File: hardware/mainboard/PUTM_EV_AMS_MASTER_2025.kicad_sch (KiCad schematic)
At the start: 41 parts, among them IC11 ISO6760, IC7 ISO6760, IC8 3.3V/0.5A, J1 M80-5100642, J10 M300-MV10345M1, J12 M80-51034XX, J2 USB_C_Receptacle_USB2.0_14P, J3 M80-51014XX, J4 FTSH-107-01-L-D-K, J5 M80-51004XX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

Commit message: sync
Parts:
- removed J2: USB_C_Receptacle_USB2.0_14P, Connector_USB:USB_C_Receptacle_JAE_DX07S024WJ3R400, symbol Connector:USB_C_Receptacle_USB2.0_14P
- removed J3: M80-51014XX, Samacsys:M80-51014YY, symbol Samacsys_kicad_sym:M80-51014XX
- removed R91, R92: 5.1k, Resistor_SMD:R_0603_1608Metric, symbol Device:R_Small
- removed T1: >100kHz, Samacsys:SOP254P914X350-4N, symbol Samacsys_kicad_sym:ESMIT-4180_C
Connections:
- net TSMS: now also J12.15 (Pin_15); no longer J12.1 (Pin_1)
- net ISO_COM_MOSI: no longer names the net of IC7.12 (OUTD)
- net ISO_COM_SCK: no longer names the net of IC7.11 (OUTE)
- net MCU/COM_MOSI: no longer names the net of IC7.5 (IND)
- net MCU/COM_SCK: no longer names the net of IC7.6 (INE)
- net MCU/~{COM_CS}: no longer names the net of IC7.7 (INF)
- net ~{ISO_COM_CS}: no longer names the net of IC7.10 (OUTF)
- no-connect marks 27 -> 26
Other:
- sheet Connectivity ports: added none; removed EX_D+, EX_D-
- sheet Fan Control ports: added none; removed FAN5_CTRL, FAN5_DRAIN, FAN6_CTRL, FAN6_DRAIN, FAN7_CTRL, FAN7_DRAIN
- sheet MCU ports: added none; removed COM_MOSI, COM_SCK, EN_12V, FAN5_CTRL, FAN6_CTRL, FAN7_CTRL, PG_12V, ~{COM_CS}
- sheet Power ports: added none; removed EN_12V, PG_12V
- note removed: "USB CONNECTOR"

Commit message: schematic?
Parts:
- removed C39, C44, C45, C46, C47, C48: 100nF, Capacitor_SMD:C_0603_1608Metric, symbol Device:C_Small
- removed C40, C59, C77: 22uF, Capacitor_SMD:C_0805_2012Metric, symbol Device:C_Small
- removed F6, F7: 5V/0.5A, Fuse:Fuse_0805_2012Metric, symbol Device:Polyfuse_Small
- removed IC11, IC7: ISO6760, Package_SO:SOIC-16W_7.5x10.3mm_P1.27mm, symbol Samacsys_kicad_sym:ISO6760
- removed IC8: 3.3V/0.5A, Package_TO_SOT_SMD:SOT-23-5, symbol AP7365-33YRG-13:AP7365-33YRG-13
- removed J12: M80-51034XX, Samacsys:M80-51034YY, symbol Samacsys_kicad_sym:M80-51034XX
- removed R22: 200, Resistor_SMD:R_0603_1608Metric, symbol Device:R_Small
- removed TP4, TP5, TP6, TP7, TP8: TestPoint_Small, TestPoint:TestPoint_THTPad_D1.0mm_Drill0.5mm, symbol Connector:TestPoint_Small
- removed U4: UCC12040DVE, Package_SO:SOIC-16W_7.5x10.3mm_P1.27mm, symbol Samacsys_kicad_sym:UCC12040DVE
- added C81: 100pF, Capacitor_SMD:C_0603_1608Metric, symbol Device:C_Small
- added D21, D22: 3.6V/400W, Package_TO_SOT_SMD:SOT-23-6, symbol Power_Protection:ESDA5V3SC5
- added D23: 5.3V/400W, Package_TO_SOT_SMD:SOT-23-3, symbol Power_Protection:ESDA5V3L
- added J2: M80-5102042, Samacsys:M80-51020YY, symbol Samacsys_kicad_sym:M80-5102042
- added J3: M80-5100842, Samacsys:M80-51008YY, symbol Samacsys_kicad_sym:M80-5100842
- added T1: SM91502ALE, Samacsys:SOP254P927X572-6N, symbol Samacsys_kicad_sym:SM91502ALE
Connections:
- net GNDISO is gone; now on net GND: J8.4 (Pin_4)
- net AIR_M_DETECTION: now also J2.15
- net AIR_PRE_DETECTION: now also J2.14
- net AIR_P_DETECTION: now also J2.13
- net CANFD1+: now also J2.3
- net CANFD1-: now also J2.4
- net CANFD2+: now also J2.5
- net CANFD2-: now also J2.6
- net CAR_I: now also D23.1 (K)
- net CCO+: now also T1.3 (PRI_3)
- net CCO-: now also T1.1 (PRI_1)
- net CHARGER_DETECTION: now also J2.12
- net FAN1-: now also J3.1
- net FAN2-: now also J3.2
- net FAN3-: now also J3.3
- net FAN4-: now also J3.4
- net GND: now also C81.2, D21.2 (K), D21.5 (NC), D22.2 (K), D22.5 (NC), D23.3 (A), J2.11, J2.19, J2.20
- net NRST: now also D21.4 (A)
- net SAFETY_IN: now also J2.8
- net SAFETY_OUT: now also J2.7
- net SWCLK: now also D21.3 (A)
- net SWDIO: now also D21.1 (A)
- net TSMS: now also J2.18
- net UART_RX: now also D22.1 (A)
- net UART_TX: now also D21.6 (A)
- net VDD: now also J2.10
- net +3.3V renamed +3.3VIO
- net +3.3VIO: now also D22.3 (A)
- net +5VISO: no longer names the net of J8.3 (Pin_3)
- net ACU+ renamed IsolationBarrier/ACU_IN+
- net ACU- renamed IsolationBarrier/ACU_IN-
- net CAR+ renamed IsolationBarrier/CAR_IN+
- net CAR- renamed IsolationBarrier/CAR_IN-
- net CAR_I_REF renamed +5VA
- net +5VA: now also D23.2 (K)
- new net: C81.1, T1.5 (SEC_2)
- new net +24V: J3.5, J3.6, J3.7, J3.8
- new net +8V: J2.9
- new net D+: J2.2
- new net D-: J2.1
- new net Isolated SPI/OUT+: T1.4 (SEC_1)
- new net Isolated SPI/OUT-: T1.6 (SEC_3)
- new net VBUS+: J2.17
- no-connect marks 26 -> 12
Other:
- sheet Isolated ADC renamed ADC
- added sheet IsolationBarrier (IsolationBarrier.kicad_sch)
- sheet ADC: file IsolatedADC.kicad_sch -> ADC.kicad_sch
- sheet ADC ports: added none; removed CAR_I_REF
- sheet Connectivity ports: added EX_D+, EX_D-, FTDI_RX, FTDI_TX; removed EX_USB_D+, EX_USB_D-, UC_D+, UC_D-
- sheet Isolated SPI ports: added RX, TX; removed MISO, MOSI, SCK, SPI_RDY, ~{CS}
- sheet MCU ports: added DETECT_USB, SIGNAL_LED_ERR, SIGNAL_LED_OK, SIGNAL_LED_WRN, UART_COM_RX, UART_COM_TX, UART_DEBUG_RX, UART_DEBUG_TX, UART_USB_RX, UART_USB_TX; removed COM_MISO, D+, D-, SIGNAL_LED_1, SIGNAL_LED_2, SIGNAL_LED_3, SPI_RDY, UART_RX, UART_TX
- sheet Power ports: added VBUS_SENSE; removed none
- sheet Safety ports: added none; removed DASH_LED_ERROR
- note added: "ADC"
- note added: "AIR"
- note added: "COM"
- note added: "CURRENT"
- note added: "FAN"
- note added: "USBGND"
- note removed: "ADC AND SPI"
- note removed: "AIR CONNECTORS"
- note removed: "AIR CONTROL"
- note removed: "CONNECTORS"
- note removed: "FAN CONNECTORS"
- note removed: "FAN CONTROL"
- note removed: "GALVANIC ISOLATION"
- note removed: "ISO POWER"
- note removed: "SHARED"
- note removed: "TI_IC ONLY"
- moved on the sheet: D1, D2, D3, D6, J1, J10, J4, J5, J7, J8, R27, R31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

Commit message: sync
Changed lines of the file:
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@@
+		)
+	)
+	(label "ADC_MOSI"
+		(at 182.88 81.28 180)
+		(effects
+			(font
+				(size 0.508 0.508)
+			)
+			(justify right bottom)
 		)
 	)
@@
 	)
 	(label "ADC_MISO"
-		(at 182.88 81.28 180)
+		(at 182.88 78.74 180)
 		(effects
 			(font
@@
 		)
 	)
+	(label "ADC_SCK"
+		(at 182.88 83.82 180)
+		(effects
+			(font
+				(size 0.508 0.508)
+			)
+			(justify right bottom)
+		)
+	)
 	(label "FC1"
 		(at 182.88 259.08 180)
@@
 		)
 	)
-	(label "ADC_MISO"
-		(at 182.88 78.74 180)
-		(effects
-			(font
-				(size 0.508 0.508)
-			)
-			(justify right bottom)
-		)
-	)
 	(label "CTX1"
 		(at 222.25 187.96 0)
@@
 		)
 	)
-	(label "ADC_MISO"
-		(at 182.88 83.82 180)
-		(effects
-			(font
-				(size 0.508 0.508)
-			)
-			(justify right bottom)
-		)
-	)
 	(label "NRST"
 		(at 335.28 88.9 180)
@@
 		)
 	)
+	(netclass_flag ""
+		(length 2.54)
+		(shape round)
+		(at 75.2666 149.86 0)
+		(fields_autoplaced yes)
+		(effects
+			(font
+				(size 1.27 1.27)
+			)
+			(justify left bottom)
+		)
+		(property "Netclass" "120Ohm"
+			(at 74.657 147.32 0)
+			(effects
+				(font
+					(size 1.27 1.27)
+				)
+				(justify right)
+			)
+		)
+		(property "Component Class" ""
+			(at 348.3166 57.15 0)
+			(effects
+				(font
+					(size 1.27 1.27)
+					(italic yes)
+				)
+				(justify left)
+			)
+		)
+	)
+	(netclass_flag ""
+		(length 2.54)
+		(shape round)
+		(at 75.2666 152.4 180)
+		(fields_autoplaced yes)
+		(effects
+			(font
+				(size 1.27 1.27)
+			)
+			(justify right bottom)
+		)
+		(property "Netclass" "120Ohm"
+			(at 74.657 154.94 0)
+			(effects
+				(font
+					(size 1.27 1.27)
+				)
+				(justify right)
+			)
+		)
+		(property "Component Class" ""
+			(at 348.3166 245.11 0)
+			(effects
+				(font
+					(size 1.27 1.27)
+					(italic yes)
+				)
+				(justify left)
+			)
+		)
+	)

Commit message: sync
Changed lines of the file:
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@@
+		)
+	)
+	(label "AMSERR"
+		(at 222.25 226.06 0)
+		(effects
+			(font
+				(size 0.508 0.508)
+			)
+			(justify left bottom)
 		)
 	)
@@
 		)
 	)
-	(label "VUSB"
+	(label "DETVUSB"
 		(at 222.25 124.46 0)
 		(effects
 			(font
+				(size 0.508 0.508)
+			)
+			(justify left bottom)
+		)
+	)
+	(label "DETERR"
+		(at 222.25 228.6 0)
+		(effects
+			(font

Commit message: sync
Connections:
- net +8V: now also J2.17; no longer J2.9
- net AIR_M_DETECTION: now also J2.16; no longer J2.15
- net AIR_PRE_DETECTION: now also J2.15; no longer J2.14
- net AIR_P_DETECTION: now also J2.14; no longer J2.13
- net CHARGER_DETECTION: now also J2.13; no longer J2.12
- net GND: now also J2.7
- net SAFETY_IN: now also J2.18; no longer J2.8
- net SAFETY_OUT: now also J2.8; no longer J2.7
- net TSMS: now also J2.9; no longer J2.18
- net VBUS+: now also J2.12; no longer J2.17
- no-connect marks 12 -> 11

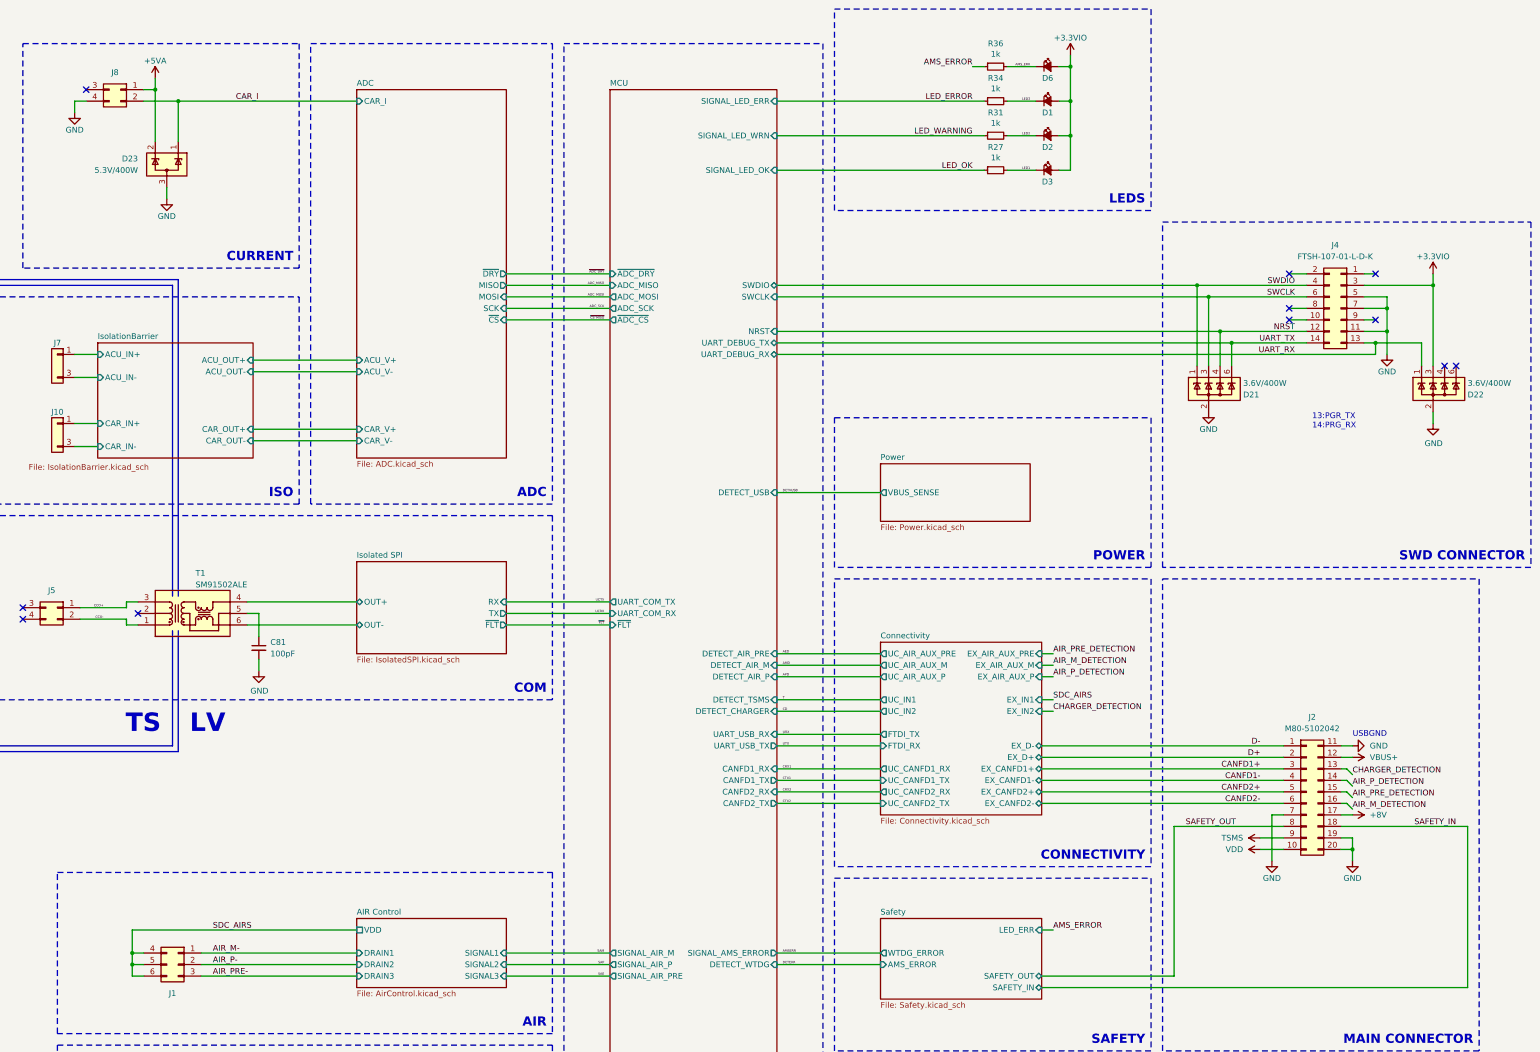
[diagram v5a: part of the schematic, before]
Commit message: hardware routing done, only touch ups will be needed if the board is aproved
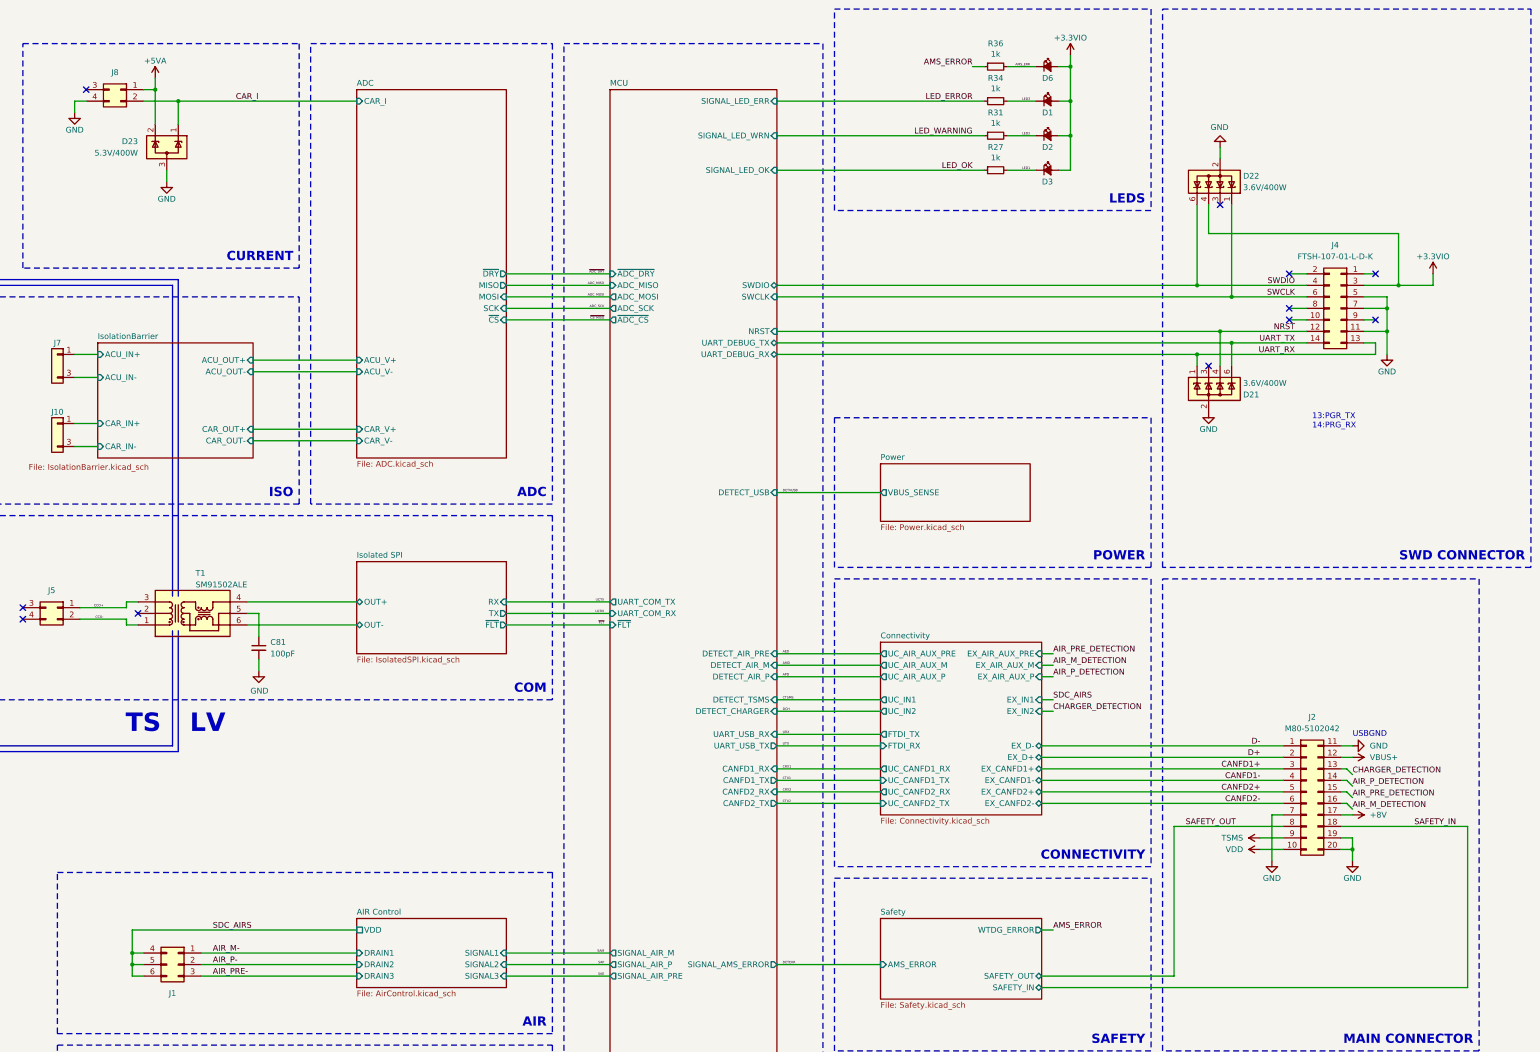
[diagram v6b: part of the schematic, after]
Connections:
- net +3.3VIO: now also D22.4 (A); no longer D22.3 (A)
- net SWCLK: now also D22.1 (A); no longer D21.3 (A)
- net SWDIO: now also D22.6 (A); no longer D21.1 (A)
- net UART_RX: now also D21.1 (A); no longer D22.1 (A)
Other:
- sheet MCU ports: added none; removed DETECT_WTDG
- sheet Safety ports: added none; removed LED_ERR
- moved on the sheet: D22, D23

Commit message: isolation with every thing
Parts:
- added D27: 5.3V/400W, Package_TO_SOT_SMD:SOT-23-3, symbol Power_Protection:ESDA5V3L
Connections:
- net +8V is gone; now on net +3.3VIO: J2.17
- net SDC_AIRS is gone; now on net +24V: J1.4 (Pin_4), J1.5 (Pin_5), J1.6 (Pin_6)
- net +3.3VIO: now also D27.1 (K)
- net GND: now also D27.3 (A); no longer J2.19, J2.7
- net CANFD1+ renamed EX_CANFD1_RX
- net CANFD1- renamed EX_CANFD1_TX
- net CANFD2+ renamed EX_CANFD2_RX
- net CANFD2- renamed EX_CANFD2_TX
- net SAFETY_IN renamed +5VIO
- net +5VIO: now also D27.2 (K)
- net SAFETY_OUT: no longer names the net of J2.8
- net TSMS renamed ERROR_RELAY-
- new net TSMS_DETECTION: J2.7
- no-connect marks 11 -> 13
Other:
- sheet AIR Control ports: added none; removed VDD
- sheet Connectivity ports: added EX_CANFD1_RX, EX_CANFD1_TX, EX_CANFD2_RX, EX_CANFD2_TX, ~{FTDI_RST}; removed EX_CANFD1+, EX_CANFD1-, EX_CANFD2+, EX_CANFD2-
- sheet MCU ports: added ~{FTDI_RST}; removed none
- sheet Safety ports: added ERROR_RELAY-; removed SAFETY_IN, SAFETY_OUT

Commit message: isolated side, choose most components, some master changes tbc
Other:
- note added: "use cheaper connectors for ioslation pcb interface - 2mm spacing between pins"
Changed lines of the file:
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@@
 		)
 	)
+	(text "use cheaper connectors for ioslation pcb interface - 2mm spacing between pins"
+		(exclude_from_sim no)
+		(at 100.33 202.184 0)
+		(effects
+			(font
+				(size 1.27 1.27)
+			)
+		)
+	)
 	(text "COM"
 		(exclude_from_sim no)
@@
 	)
 	(junction
-		(at 361.95 198.12)
+		(at 358.14 67.31)
 		(diameter 0)
 		(color 0 0 0 0)
 	)
 	(junction
-		(at 358.14 78.74)
+		(at 361.95 198.12)
 		(diameter 0)
 		(color 0 0 0 0)
@@
 	(wire
 		(pts
-			(xy 358.14 78.74) (xy 365.76 78.74)
-		)
-		(stroke
-			(width 0)
-			(type default)
-		)
-	)
-	(wire
-		(pts
 			(xy 220.98 193.04) (xy 243.84 193.04)
 		)
@@
 	(wire
 		(pts
+			(xy 316.23 109.22) (xy 316.23 106.68)
+		)
+		(stroke
+			(width 0)
+			(type default)
+		)
+	)
+	(wire
+		(pts
 			(xy 78.74 259.08) (xy 81.28 259.08)
 		)
@@
 	(wire
 		(pts
-			(xy 365.76 76.2) (xy 365.76 78.74)
+			(xy 358.14 64.77) (xy 358.14 67.31)
 		)
 		(stroke
@@
 		(lib_name "GND_28")
 		(lib_id "power:GND")
-		(at 316.23 106.68 0)
+		(at 316.23 109.22 0)
 		(mirror y)
 		(unit 1)
@@
 		(dnp no)
 		(property "Reference" "#PWR034"
-			(at 316.23 113.03 0)
+			(at 316.23 115.57 0)
 			(effects
 				(font
@@
 		)
 		(property "Value" "GND"
-			(at 316.23 110.49 0)
+			(at 316.23 113.03 0)
 			(effects
 				(font
@@
 		)
 		(property "Footprint" ""
-			(at 316.23 106.68 0)
+			(at 316.23 109.22 0)
 			(effects
 				(font
@@
 		)
 		(property "Datasheet" ""
-			(at 316.23 106.68 0)
+			(at 316.23 109.22 0)
 			(effects
 				(font
@@
 		)
 		(property "Description" ""
-			(at 316.23 106.68 0)
+			(at 316.23 109.22 0)
 			(effects
 				(font
@@
 	(symbol
 		(lib_id "power:+3.3V")
-		(at 365.76 76.2 0)
+		(at 358.14 64.77 0)
 		(unit 1)
 		(exclude_from_sim no)
@@
 		(dnp no)
 		(property "Reference" "#PWR073"
-			(at 365.76 80.01 0)
+			(at 358.14 68.58 0)
 			(effects
 				(font
@@
 		)
 		(property "Value" "+3.3VIO"
-			(at 365.76 72.39 0)
+			(at 358.14 60.96 0)
 			(effects
 				(font
@@
 		)
 		(property "Footprint" ""
-			(at 365.76 76.2 0)
+			(at 358.14 64.77 0)
 			(effects
 				(font
@@
 		)
 		(property "Datasheet" ""
-			(at 365.76 76.2 0)
+			(at 358.14 64.77 0)
 			(effects
 				(font
@@
 		)
 		(property "Description" ""
-			(at 365.76 76.2 0)
+			(at 358.14 64.77 0)
 			(effects
 				(font
